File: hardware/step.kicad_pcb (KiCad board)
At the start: 4 copper layers, 150 x 35 mm, 127 parts, among them J101 WAGO 2065-100, J102 WAGO 2065-100, J103 Cortex, J1901 2x05_Horizontal, J2001 2x05_Horizontal, J201 WAGO 2065-100, J202 WAGO 2065-100, J203 WAGO 2065-100, J204 WAGO 2065-100, J301 WAGO 2065-100, J302 WAGO 2065-100, J303 WAGO 2065-100, J304 WAGO 2065-100, J401 WAGO 2065-100, J402 WAGO 2065-100, J403 WAGO 2065-100, J404 WAGO 2065-100, J501 WAGO 2065-100, J502 WAGO 2065-100, J503 WAGO 2065-100, J504 WAGO 2065-100, SW101 SKSG, SW102 SKSG, U101 ATSAMD51J, U102 TPS78433QWDRBRQ1, U1901 THVD2442, U2001 THVD2442, U201 TMC2130-LA, U301 TMC2130-LA, U401 TMC2130-LA, U501 TMC2130-LA, Y101 32k768

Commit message: Good Bye Imperial
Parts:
- C101: renamed from C107; footprint V2_Capacitor_SMD:C_0603 -> V2_Capacitor_SMD:C_1608
- C102: renamed from C108; footprint V2_Capacitor_SMD:C_0603 -> V2_Capacitor_SMD:C_1608
- C103: renamed from C110; footprint V2_Capacitor_SMD:C_0805 -> V2_Capacitor_SMD:C_2012
- C104: renamed from C101; footprint V2_Capacitor_SMD:C_0603 -> V2_Capacitor_SMD:C_1608
- C105: renamed from C111; footprint V2_Capacitor_SMD:C_0805 -> V2_Capacitor_SMD:C_2012
- C106: renamed from C102; footprint V2_Capacitor_SMD:C_0603 -> V2_Capacitor_SMD:C_1608
- C107: renamed from C103; footprint V2_Capacitor_SMD:C_0603 -> V2_Capacitor_SMD:C_1608
- C108: renamed from C104; footprint V2_Capacitor_SMD:C_0603 -> V2_Capacitor_SMD:C_1608
- C109: renamed from C105; footprint V2_Capacitor_SMD:C_0603 -> V2_Capacitor_SMD:C_1608
- C110: renamed from C106; footprint V2_Capacitor_SMD:C_0603 -> V2_Capacitor_SMD:C_1608
- C111: renamed from C109; footprint V2_Capacitor_SMD:C_0603 -> V2_Capacitor_SMD:C_1608
- C1901, C2001, C208, C308, C408, C508: footprint V2_Capacitor_SMD:C_0603 -> V2_Capacitor_SMD:C_1608
- C201: renamed from C205; footprint V2_Capacitor_SMD:C_0603 -> V2_Capacitor_SMD:C_1608
- C202: renamed from C206; footprint V2_Capacitor_SMD:C_0603 -> V2_Capacitor_SMD:C_1608
- C203: renamed from C201; footprint V2_Capacitor_SMD:C_0603 -> V2_Capacitor_SMD:C_1608
- C204: renamed from C207; footprint V2_Capacitor_SMD:C_0603 -> V2_Capacitor_SMD:C_1608
- C206: renamed from C203; footprint V2_Capacitor_SMD:C_1210 -> V2_Capacitor_SMD:C_3225
- C207: renamed from C204; footprint V2_Capacitor_SMD:C_1210 -> V2_Capacitor_SMD:C_3225
- C301: renamed from C305; footprint V2_Capacitor_SMD:C_0603 -> V2_Capacitor_SMD:C_1608
- C302: renamed from C306; footprint V2_Capacitor_SMD:C_0603 -> V2_Capacitor_SMD:C_1608
- C303: renamed from C301; footprint V2_Capacitor_SMD:C_0603 -> V2_Capacitor_SMD:C_1608
- C304: renamed from C307; footprint V2_Capacitor_SMD:C_0603 -> V2_Capacitor_SMD:C_1608
- C306: renamed from C303; footprint V2_Capacitor_SMD:C_1210 -> V2_Capacitor_SMD:C_3225
- C307: renamed from C304; footprint V2_Capacitor_SMD:C_1210 -> V2_Capacitor_SMD:C_3225
- C401: renamed from C405; footprint V2_Capacitor_SMD:C_0603 -> V2_Capacitor_SMD:C_1608
- C402: renamed from C406; footprint V2_Capacitor_SMD:C_0603 -> V2_Capacitor_SMD:C_1608
- C403: renamed from C401; footprint V2_Capacitor_SMD:C_0603 -> V2_Capacitor_SMD:C_1608
- C404: renamed from C407; footprint V2_Capacitor_SMD:C_0603 -> V2_Capacitor_SMD:C_1608
- C406: renamed from C403; footprint V2_Capacitor_SMD:C_1210 -> V2_Capacitor_SMD:C_3225
- C407: renamed from C404; footprint V2_Capacitor_SMD:C_1210 -> V2_Capacitor_SMD:C_3225
- C501: renamed from C505; footprint V2_Capacitor_SMD:C_0603 -> V2_Capacitor_SMD:C_1608
- C502: renamed from C506; footprint V2_Capacitor_SMD:C_0603 -> V2_Capacitor_SMD:C_1608
- C503: renamed from C501; footprint V2_Capacitor_SMD:C_0603 -> V2_Capacitor_SMD:C_1608
- C504: renamed from C507; footprint V2_Capacitor_SMD:C_0603 -> V2_Capacitor_SMD:C_1608
- C506: renamed from C503; footprint V2_Capacitor_SMD:C_1210 -> V2_Capacitor_SMD:C_3225
- C507: renamed from C504; footprint V2_Capacitor_SMD:C_1210 -> V2_Capacitor_SMD:C_3225
- D103: renamed from D101; footprint V2_LED:LED_0603 -> V2_LED:LED_1608
- R101: renamed from R105; footprint V2_Resistor_SMD:R_0603 -> V2_Resistor_SMD:R_1608
- R102: renamed from R104; footprint V2_Resistor_SMD:R_0603 -> V2_Resistor_SMD:R_1608
- R103: renamed from R101; footprint V2_Resistor_SMD:R_0603 -> V2_Resistor_SMD:R_1608
- R104: renamed from R103; footprint V2_Resistor_SMD:R_0603 -> V2_Resistor_SMD:R_1608
- R105: renamed from R102; footprint V2_Resistor_SMD:R_0603 -> V2_Resistor_SMD:R_1608
- R1901, R2001, R201, R301, R401, R501: footprint V2_Resistor_SMD:R_0603 -> V2_Resistor_SMD:R_1608
- R202, R203, R302, R303, R402, R403, R502, R503: footprint V2_Resistor_SMD:R_0805 -> V2_Resistor_SMD:R_2012
- TVS101: renamed from TVS102; footprint V2_Diode_SMD:D_0603 -> V2_Diode_SMD:D_1608
- renumbered C202 to C205, C302 to C305, C402 to C405, C502 to C505, D102 to D101, D103 to D102, H103 to H102, H105 to H103, H107 to H104, H108 to H105, H102 to H106, H104 to H107, H106 to H108, ICON105 to ICON101, ICON104 to ICON102, ICON101 to ICON103, ICON102 to ICON104, ICON103 to ICON105, INFO102 to INFO101, INFO101 to INFO102, J103 to J101, J101 to J102, J102 to J103, SW102 to SW101, SW101 to SW102, TVS101 to TVS102, U102 to U101, U101 to U102

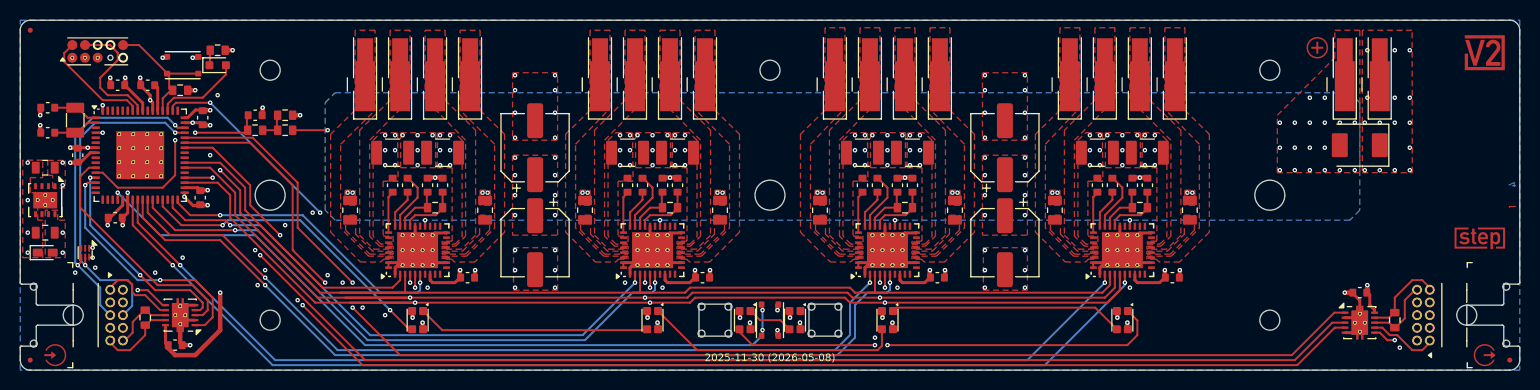
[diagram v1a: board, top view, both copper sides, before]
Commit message: Switch to 6 layer
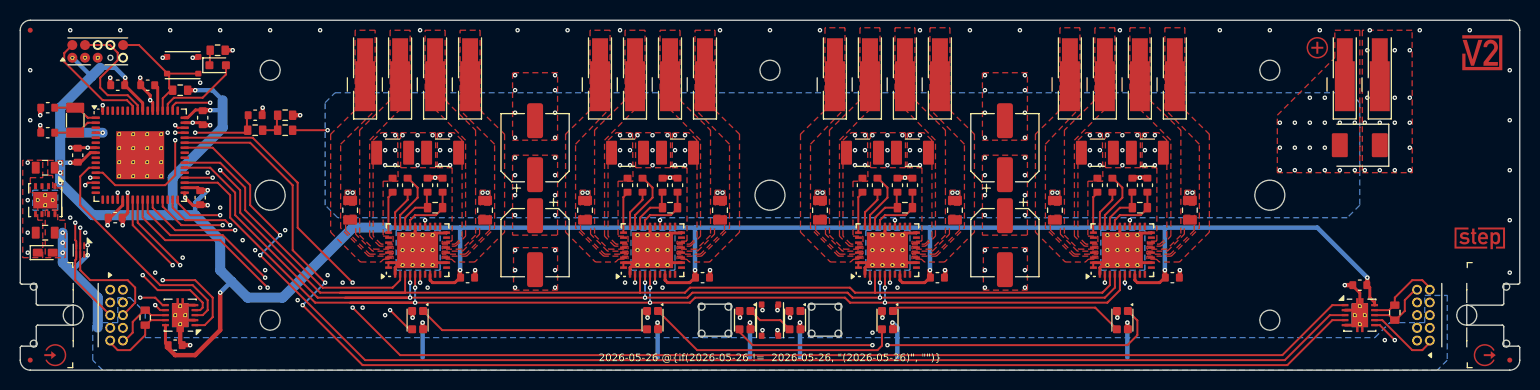
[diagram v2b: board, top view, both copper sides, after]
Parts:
- INFO102: value Layer_Numbers -> Layer_Numbers-6; footprint V2_Production:Layer_Numbers -> V2_Production:Layer_Numbers-6
- moved C2001 0.75 mm to (211.0, 106.5)
- moved R2001 0.75 mm to (214.5, 109.2)
- moved U2001 0.75 mm to (211.0, 109.5)
- moved ESD101 0.56 mm to (83.0, 103.0)
- moved ICON102 0.25 mm to (223.2, 83.2)
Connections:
- ESD101 pad 2: unconnected-(ESD101-D2-Pad2) -> /USB-
- ESD101 pad 3: unconnected-(ESD101-D1-Pad3) -> /USB+
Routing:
- net +3V3: track 51.5 -> 258.3 mm, vias 15 -> 16
- net +5V: track 4.46 -> 38.9 mm, vias 9 -> 10
- net /USB+: track 32.4 -> 30.8 mm
- net /Step-1: track 30.0 -> 28.7 mm
- net /Link Socket/RX-B: track 7.16 -> 6.41 mm
- net /USB-: track 34.1 -> 33.4 mm
- net /Link Socket/RX-A: track 8.66 -> 7.99 mm
- net /Link Plug/TX-Z: track 7.73 -> 7.64 mm, vias 0 -> 1
- net GND: vias 144 -> 176
- net /Enable: vias 6 -> 5
- added copper zone on B.Cu, net +5V
- added copper zone on In3.Cu, net GND
- added copper zone on In4.Cu, net GND
- removed copper zone on In2.Cu, net +3V3
- removed copper zone on In2.Cu, net +5V
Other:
- copper layers 4 -> 6
